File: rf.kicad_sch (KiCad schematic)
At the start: 28 parts, among them IC2 NRF51822-QFAA-R7, IC3 BAL-NRF02D3, IC4 RFX2411N, J1 U.FL-R-SMT-1_10_, Y1 ABM3B-16.000MHZ-B2-T, Y2 ADFC15-2450.00-A-T, Y3 ADFC15-2450.00-A-T

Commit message: Added FPGA power component
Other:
- title: (none) -> Radio Frequency Communication
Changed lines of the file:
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@@
 (kicad_sch (version 20230121) (generator eeschema)
   (paper "A4")
+  (title_block
+    (title "Radio Frequency Communication")
+  )
   (junction (at 53.34 110.49) (diameter 0) (color 0 0 0 0)
   )

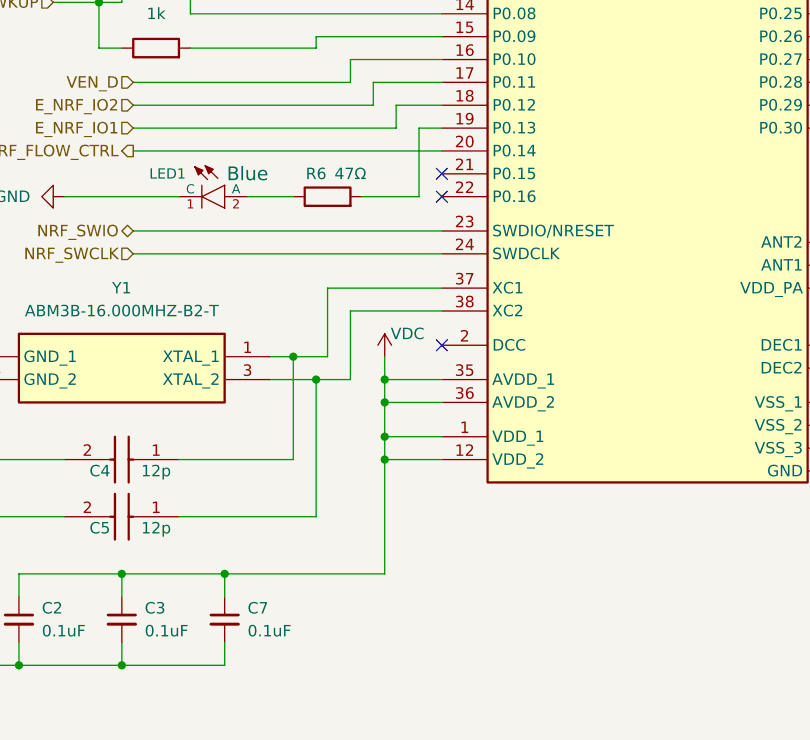
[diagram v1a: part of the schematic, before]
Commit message: Integrated MPM3833C
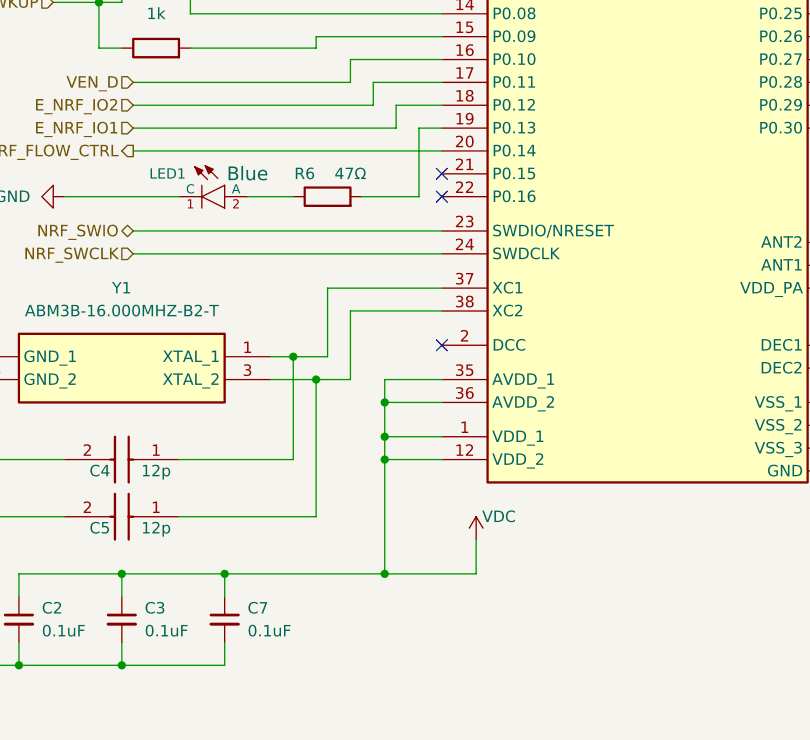
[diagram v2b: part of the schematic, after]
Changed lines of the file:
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@@
   (junction (at 151.13 120.65) (diameter 0) (color 0 0 0 0)
   )
+  (junction (at 63.5 134.62) (diameter 0) (color 0 0 0 0)
+  )
   (junction (at 15.24 128.27) (diameter 0) (color 0 0 0 0)
   )
@@
   )
   (junction (at 34.29 134.62) (diameter 0) (color 0 0 0 0)
-  )
-  (junction (at 63.5 113.03) (diameter 0) (color 0 0 0 0)
   )
   (junction (at 246.38 107.95) (diameter 0) (color 0 0 0 0)
@@
     (stroke (width 0) (type default))
   )
+  (wire (pts (xy 63.5 134.62) (xy 73.66 134.62))
+    (stroke (width 0) (type default))
+  )
   (wire (pts (xy 275.59 92.71) (xy 278.13 92.71))
     (stroke (width 0) (type default))
@@
     (stroke (width 0) (type default))
   )
-  (wire (pts (xy 63.5 110.49) (xy 63.5 113.03))
-    (stroke (width 0) (type default))
-  )
   (wire (pts (xy 69.85 52.07) (xy 67.31 52.07))
     (stroke (width 0) (type default))
@@
   )
   (wire (pts (xy 191.77 110.49) (xy 200.66 110.49))
+    (stroke (width 0) (type default))
+  )
+  (wire (pts (xy 73.66 134.62) (xy 73.66 130.81))
     (stroke (width 0) (type default))
   )
@@
   (symbol (lib_id "PCM_4ms_Resistor:47R_0402") (at 57.15 92.71 90) (unit 1)
     (in_bom yes) (on_board yes) (dnp no)
-    (property "Reference" "R6" (at 55.88 90.17 90)
+    (property "Reference" "R6" (at 54.61 90.17 90)
       (effects (font (size 1.27 1.27)))
     )
@@
     )
   )
-  (symbol (lib_id "power:VDC") (at 63.5 110.49 0) (unit 1)
+  (symbol (lib_id "power:VDC") (at 73.66 130.81 0) (unit 1)
     (in_bom yes) (on_board yes) (dnp no)
-    (property "Reference" "#PWR09" (at 63.5 113.03 0)
-      (effects (font (size 1.27 1.27)) hide)
-    )
-    (property "Value" "VDC" (at 66.04 107.95 0)
-      (effects (font (size 1.27 1.27)))
-    )
-    (property "Footprint" "" (at 63.5 110.49 0)
-      (effects (font (size 1.27 1.27)) hide)
-    )
-    (property "Datasheet" "" (at 63.5 110.49 0)
-      (effects (font (size 1.27 1.27)) hide)
-    )
+    (property "Reference" "#PWR09" (at 73.66 133.35 0)
+      (effects (font (size 1.27 1.27)) hide)
+    )
+    (property "Value" "VDC" (at 76.2 128.27 0)
+      (effects (font (size 1.27 1.27)))
+    )
+    (property "Footprint" "" (at 73.66 130.81 0)
+      (effects (font (size 1.27 1.27)) hide)
+    )
+    (property "Datasheet" "" (at 73.66 130.81 0)
+      (effects (font (size 1.27 1.27)) hide)
+    )
